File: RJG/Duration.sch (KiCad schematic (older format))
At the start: 24 parts, among them Q401 BC547, Q402 BC547, Q403 BC547, SW401 Duration Length, SW402 Reload, U101 4520, U401 4520, U402 74LS74, U403 74LS157, U404 74LS85, U405 SST39SF010, U406 74LS173

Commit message: Small improvements
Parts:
- added C402, C403, C404, C405, C406, C407: 100n, Capacitor_THT:C_Disc_D7.0mm_W2.5mm_P5.00mm, symbol Device:C
- added JP401: Overflow, symbol Jumper:SolderJumper_3_Bridged12
- renumbered JP401 to JP402, U101 to U102
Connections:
- net +5V: now also U404.2 (Ia<b), U404.3 (Ia=b), U404.4 (Ia>b), C402.2, C403.2, C404.2, C405.2, C406.2, C407.2
- net GND: now also C402.1, C403.1, C404.1, C405.1, C406.1, C407.1; no longer U404.2 (Ia<b), U404.3 (Ia=b), U404.4 (Ia>b)
- net at U404.5 (Oa>b): now also JP401.1 (A)
- net at U404.6 (Oa=b): now also JP401.3 (B); no longer C401.2
- net Rst_duration: now reaches JP402.2 (C), U102.15 (Reset)
- net at Q403.2 (B): now also R406.2; no longer R406.1
- net at C401.1, JP402.1 (A), R407.2: now also R406.1; no longer R406.2
- new net: C401.2, JP401.2 (C)
- no-connect marks 7 -> 5
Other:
- moved on the sheet: C401, JP402, Q403, R406, R407, SW401, U102B, U401C, U402C, U404

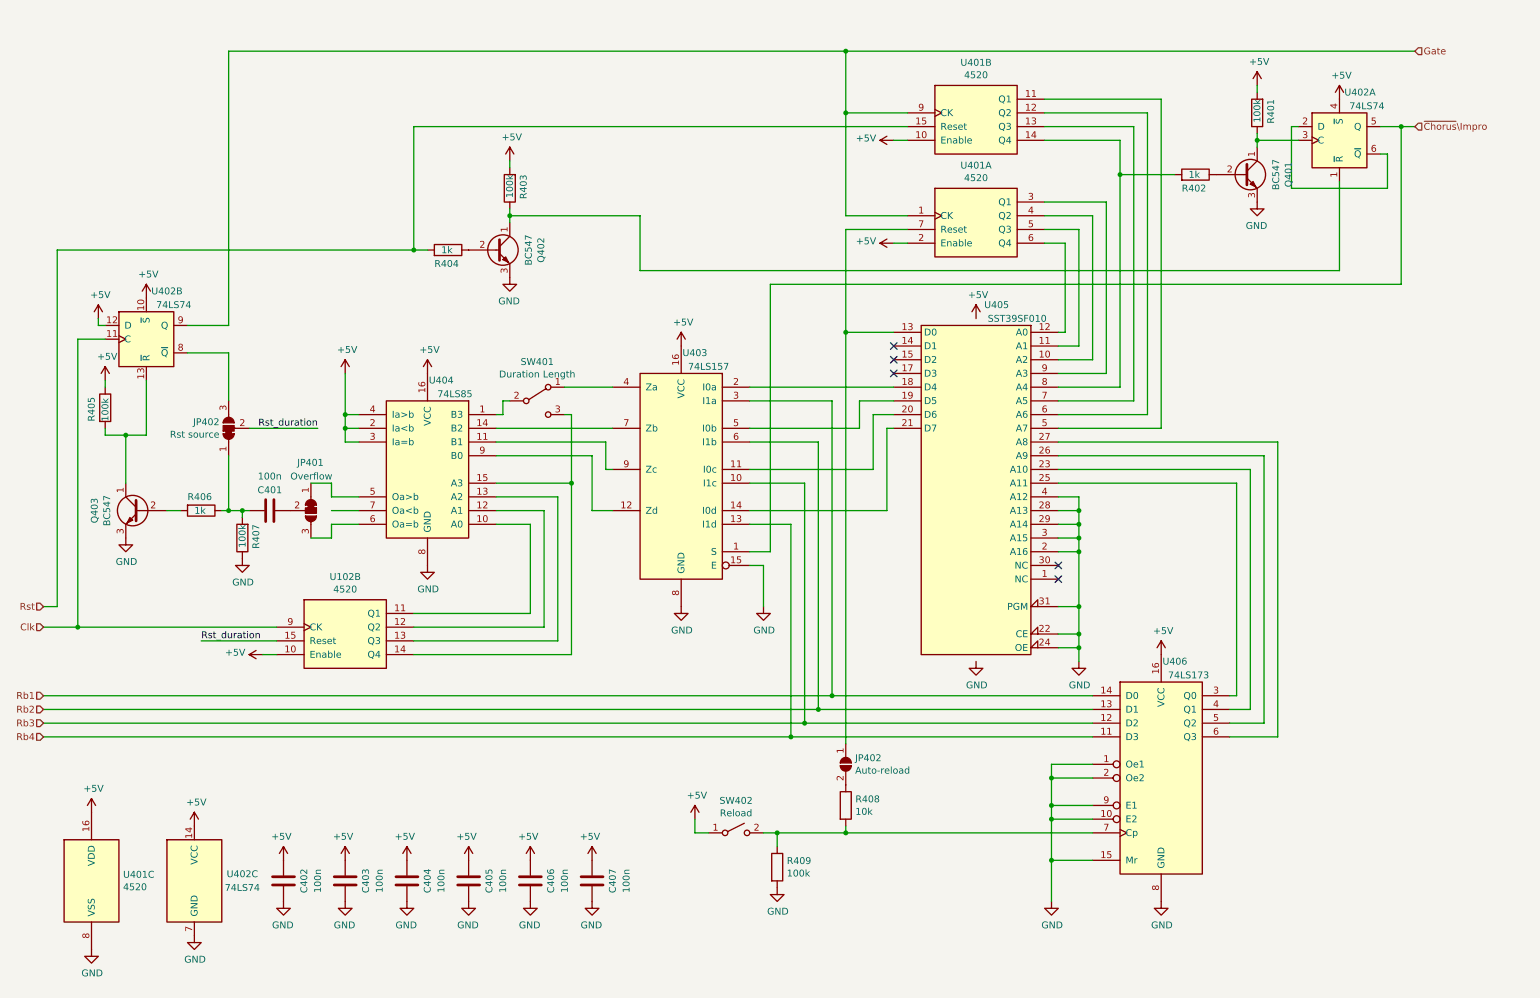
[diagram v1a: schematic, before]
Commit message: Schematic done
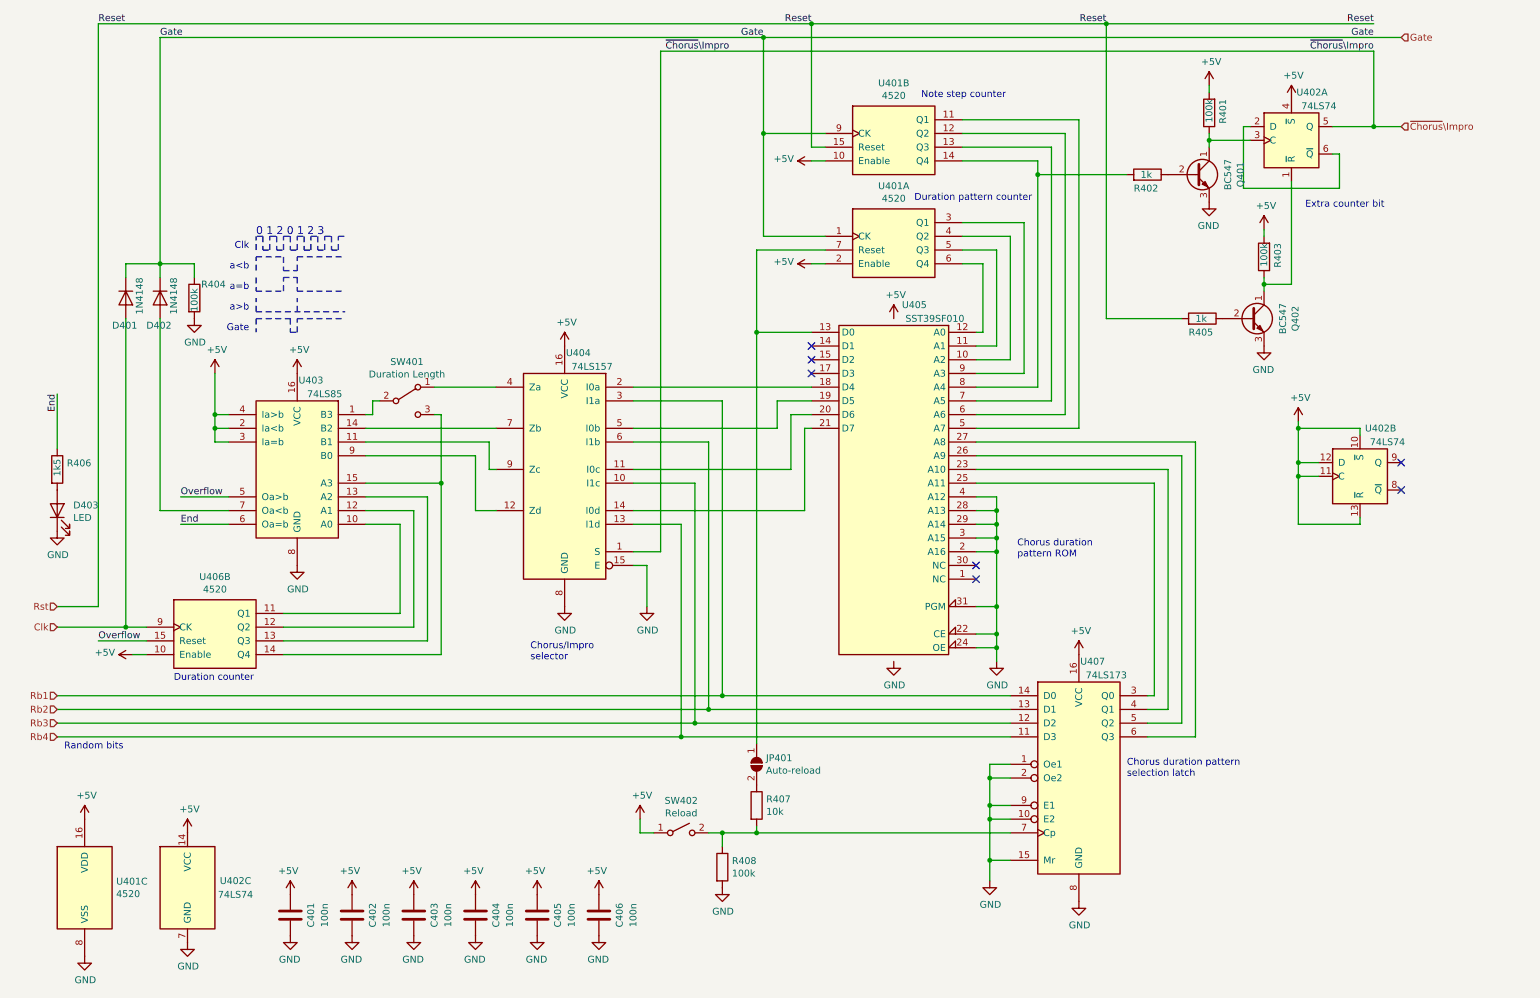
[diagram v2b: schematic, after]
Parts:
- removed C401: 100n, Capacitor_THT:C_Disc_D7.0mm_W2.5mm_P5.00mm, symbol Device:C
- removed JP401: Overflow, symbol Jumper:SolderJumper_3_Bridged12
- removed JP402: Rst source, symbol Jumper:SolderJumper_3_Bridged12
- removed Q403: BC547, Package_TO_SOT_THT:TO-92_Inline_Wide, symbol Transistor_BJT:BC547
- removed R405, R407: 100k, Resistor_THT:R_Axial_DIN0204_L3.6mm_D1.6mm_P7.62mm_Horizontal, symbol Device:R
- added D401, D402: 1N4148, Diode_THT:D_DO-35_SOD27_P7.62mm_Horizontal, symbol Device:D
- added D403: LED, LED_THT:LED_D3.0mm, symbol Device:LED
- added R404: 100k, Resistor_THT:R_Axial_DIN0204_L3.6mm_D1.6mm_P7.62mm_Horizontal, symbol Device:R
- JP401: renamed from JP402; footprint (none) -> Jumper:SolderJumper-2_P1.3mm_Open_RoundedPad1.0x1.5mm
- R406: value 1k -> 1k5
- SW401: footprint (none) -> Connector_PinHeader_2.54mm:PinHeader_1x03_P2.54mm_Vertical
- SW402: footprint (none) -> Button_Switch_THT:SW_PUSH_6mm
- renumbered C402 to C401, C403 to C402, C404 to C403, C405 to C404, C406 to C405, C407 to C406, R404 to R405, R408 to R407, R409 to R408, U404 to U403, U403 to U404, U102 to U406, U406 to U407
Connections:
- net Rst_duration is gone; now on net Overflow: U406.15 (Reset)
- net +5V: now also U402.11 (C), U402.13 (~R)
- net Clk: now also D401.2 (A); no longer U402.11 (C)
- net GND: now also D403.1 (K), R404.2
- net Gate: now also D401.1 (K), D402.1 (K), R404.1; no longer U402.9 (Q)
- net Overflow: now reaches U403.5 (Oa>b)
- net End: now reaches U403.6 (Oa=b)
- net End: now also R406.1
- net at U403.7 (Oa<b): now also D402.2 (A)
- net at R406.2: now also D403.2 (A)
- no-connect marks 5 -> 7
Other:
- note added: "0 1 2 0 1 2 3"
- note added: "Chorus duration pattern\nselection latch"
- note added: "Chorus duration\npattern ROM"
- note added: "Chorus/Impro\nselector"
- note added: "Clk"
- note added: "Duration counter"
- note added: "Duration pattern counter"
- note added: "Extra counter bit"
- note added: "Gate"
- note added: "Note step counter"
- note added: "Random bits"
- note added: "a<b"
- note added: "a=b"
- note added: "a>b"
- moved on the sheet: C401, C402, C403, C404, C405, C406, JP401, Q401, Q402, R401, R402, R403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

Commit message: Layout improvment
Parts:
- D403: footprint LED_THT:LED_D3.0mm -> LED_SMD:LED_1206_3216Metric_ReverseMount_Hole1.8x2.4mm
- R401, R403: footprint Resistor_THT:R_Axial_DIN0204_L3.6mm_D1.6mm_P7.62mm_Horizontal -> Resistor_THT:R_Axial_DIN0204_L3.6mm_D1.6mm_P2.54mm_Vertical
- R402, R405: value 1k -> 10k; footprint Resistor_THT:R_Axial_DIN0204_L3.6mm_D1.6mm_P7.62mm_Horizontal -> Resistor_THT:R_Axial_DIN0204_L3.6mm_D1.6mm_P2.54mm_Vertical
- R406: value 1k5 -> 1k; footprint Resistor_THT:R_Axial_DIN0204_L3.6mm_D1.6mm_P7.62mm_Horizontal -> Resistor_SMD:R_1206_3216Metric_Pad1.42x1.75mm_HandSolder
- U405: footprint Package_LCC:PLCC-32_11.4x14.0mm_P1.27mm -> telec:PLCC-32_THT-Socket
- renumbered U406 to U102
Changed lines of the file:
@@
 F 0 "U405" H 6700 5400 50  0000 C CNN
 F 1 "SST39SF010" H 6550 5300 50  0000 C CNN
-F 2 "Package_LCC:PLCC-32_11.4x14.0mm_P1.27mm" H 6850 4300 50  0001 C CNN
+F 2 "telec:PLCC-32_THT-Socket" H 6850 4300 50  0001 C CNN
 F 3 "http://ww1.microchip.com/downloads/en/DeviceDoc/25022B.pdf" H 6850 4300 50  0001 C CNN
 	1    6850 4000
@@
 P 1900 4950
 AR Path="/5F436EFF" Ref="U?"  Part="1"
-AR Path="/5F425067/5F436EFF" Ref="U406"  Part="2"
-F 0 "U406" H 1900 5317 50  0000 C CNN
+AR Path="/5F425067/5F436EFF" Ref="U102"  Part="2"
+F 0 "U102" H 1900 5317 50  0000 C CNN
 F 1 "4520" H 1900 5226 50  0000 C CNN
 F 2 "Package_DIP:DIP-16_W7.62mm_LongPads" H 1900 4950 50  0001 C CNN
@@
 AR Path="/5F425067/5F8F2AF1" Ref="R405"  Part="1"
 F 0 "R405" V 9000 2600 50  0000 L CNN
-F 1 "1k" V 9100 2650 50  0000 L CNN
-F 2 "Resistor_THT:R_Axial_DIN0204_L3.6mm_D1.6mm_P7.62mm_Horizontal" V 9030 2700 50  0001 C CNN
+F 1 "10k" V 9100 2650 50  0000 L CNN
+F 2 "Resistor_THT:R_Axial_DIN0204_L3.6mm_D1.6mm_P2.54mm_Vertical" V 9030 2700 50  0001 C CNN
 F 3 "~" H 9100 2700 50  0001 C CNN
 	1    9100 2700
@@
 F 0 "R403" V 9450 2150 50  0000 L CNN
 F 1 "100k" V 9550 2150 50  0000 L CNN
-F 2 "Resistor_THT:R_Axial_DIN0204_L3.6mm_D1.6mm_P7.62mm_Horizontal" V 9480 2250 50  0001 C CNN
+F 2 "Resistor_THT:R_Axial_DIN0204_L3.6mm_D1.6mm_P2.54mm_Vertical" V 9480 2250 50  0001 C CNN
 F 3 "~" H 9550 2250 50  0001 C CNN
 	1    9550 2250
@@
 AR Path="/5F425067/5FB2C32F" Ref="R402"  Part="1"
 F 0 "R402" V 8600 1550 50  0000 L CNN
-F 1 "1k" V 8700 1600 50  0000 L CNN
-F 2 "Resistor_THT:R_Axial_DIN0204_L3.6mm_D1.6mm_P7.62mm_Horizontal" V 8630 1650 50  0001 C CNN
+F 1 "10k" V 8700 1600 50  0000 L CNN
+F 2 "Resistor_THT:R_Axial_DIN0204_L3.6mm_D1.6mm_P2.54mm_Vertical" V 8630 1650 50  0001 C CNN
 F 3 "~" H 8700 1650 50  0001 C CNN
 	1    8700 1650
@@
 F 0 "R401" V 9050 1100 50  0000 L CNN
 F 1 "100k" V 9150 1100 50  0000 L CNN
-F 2 "Resistor_THT:R_Axial_DIN0204_L3.6mm_D1.6mm_P7.62mm_Horizontal" V 9080 1200 50  0001 C CNN
+F 2 "Resistor_THT:R_Axial_DIN0204_L3.6mm_D1.6mm_P2.54mm_Vertical" V 9080 1200 50  0001 C CNN
 F 3 "~" H 9150 1200 50  0001 C CNN
 	1    9150 1200
@@
 F 0 "D403" V 789 3983 50  0000 R CNN
 F 1 "LED" V 698 3983 50  0000 R CNN
-F 2 "LED_THT:LED_D3.0mm" H 750 4100 50  0001 C CNN
+F 2 "LED_SMD:LED_1206_3216Metric_ReverseMount_Hole1.8x2.4mm" H 750 4100 50  0001 C CNN
 F 3 "~" H 750 4100 50  0001 C CNN
 	1    750  4100
@@
 AR Path="/5F425067/60110003" Ref="R406"  Part="1"
 F 0 "R406" H 820 3846 50  0000 L CNN
-F 1 "1k5" V 750 3750 50  0000 L CNN
-F 2 "Resistor_THT:R_Axial_DIN0204_L3.6mm_D1.6mm_P7.62mm_Horizontal" V 680 3800 50  0001 C CNN
+F 1 "1k" V 750 3750 50  0000 L CNN
+F 2 "Resistor_SMD:R_1206_3216Metric_Pad1.42x1.75mm_HandSolder" V 680 3800 50  0001 C CNN
 F 3 "~" H 750 3800 50  0001 C CNN
 	1    750  3800

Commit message: Layout only needs the finishing touches!
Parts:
- R407: footprint Resistor_THT:R_Axial_DIN0204_L3.6mm_D1.6mm_P7.62mm_Horizontal -> Resistor_THT:R_Axial_DIN0204_L3.6mm_D1.6mm_P2.54mm_Vertical
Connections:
- net GND: now also U405.5 (A7), U405.6 (A6), U405.7 (A5), U405.8 (A4); no longer U405.2 (A16), U405.28 (A13), U405.29 (A14), U405.4 (A12)
- net Rb1: now also U404.10 (I1c); no longer U404.3 (I1a)
- net Rb3: now also U404.13 (I1d); no longer U404.10 (I1c)
- net Rb4: now also U404.3 (I1a); no longer U404.13 (I1d)
- net at U403.11 (B1): now also U404.12 (Zd); no longer U404.9 (Zc)
- net at U403.9 (B0): now also U404.4 (Za); no longer U404.12 (Zd)
- net at U404.11 (I0c): now also U405.18 (D4); no longer U405.20 (D6)
- net at U404.14 (I0d): now also U405.20 (D6); no longer U405.21 (D7)
- net at U404.2 (I0a): now also U405.21 (D7); no longer U405.18 (D4)
- net at SW401.1 (A): now also U404.9 (Zc); no longer U404.4 (Za)
- net at U407.3 (Q0): now also U405.12 (A0); no longer U405.25 (A11)
- net at U407.4 (Q1): now also U405.11 (A1); no longer U405.23 (A10)
- net at U407.5 (Q2): now also U405.9 (A3); no longer U405.26 (A9)
- net at U407.6 (Q3): now also U405.10 (A2); no longer U405.27 (A8)
- net at U401.4 (Q2): now also U405.27 (A8); no longer U405.10 (A2)
- net at U401.5 (Q3): now also U405.25 (A11); no longer U405.11 (A1)
- net at U401.6 (Q4): now also U405.23 (A10); no longer U405.12 (A0)
- net at U401.11 (Q1): now also U405.26 (A9); no longer U405.5 (A7)
- net at U401.12 (Q2): now also U405.28 (A13); no longer U405.6 (A6)
- net at U401.13 (Q3): now also U405.29 (A14); no longer U405.7 (A5)
- net at R402.2, U401.14 (Q4): now also U405.2 (A16); no longer U405.8 (A4)
- net at U401.3 (Q1): now also U405.4 (A12); no longer U405.9 (A3)
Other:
- note added: "Bit order doesn't\nreally matter -\noptimized for\nlayout"
- moved on the sheet: JP401, R407, R408, SW402

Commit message: Minor tweaks; added BOM
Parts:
- U102, U401: value 4520 -> 74HCT4520
- U402: value 74LS74 -> 74HCT74
- U403: value 74LS85 -> 74HCT85
- U404: value 74LS157 -> 74HCT157
- U406: renamed from U407; value 74LS173 -> 74HCT173
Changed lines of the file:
@@
 AR Path="/5F425067/5F4362FD" Ref="U402"  Part="1"
 F 0 "U402" H 9900 1750 50  0000 C CNN
-F 1 "74LS74" H 9950 1650 50  0000 C CNN
+F 1 "74HCT74" H 9950 1650 50  0000 C CNN
 F 2 "Package_DIP:DIP-14_W7.62mm_LongPads" H 9750 1400 50  0001 C CNN
 F 3 "74xx/74hc_hct74.pdf" H 9750 1400 50  0001 C CNN
@@
 AR Path="/5F425067/5F436309" Ref="U404"  Part="1"
 F 0 "U404" H 4350 4650 50  0000 C CNN
-F 1 "74LS157" H 4250 4550 50  0000 C CNN
+F 1 "74HCT157" H 4250 4550 50  0000 C CNN
 F 2 "Package_DIP:DIP-16_W7.62mm_LongPads" H 4450 3800 50  0001 C CNN
 F 3 "http://www.ti.com/lit/gpn/sn74LS157" H 4450 3800 50  0001 C CNN
@@
 P 8200 6050
 AR Path="/5F43630F" Ref="U?"  Part="1"
-AR Path="/5F425067/5F43630F" Ref="U407"  Part="1"
-F 0 "U407" H 8300 6900 50  0000 C CNN
-F 1 "74LS173" H 8400 6800 50  0000 C CNN
+AR Path="/5F425067/5F43630F" Ref="U406"  Part="1"
+F 0 "U406" H 8300 6900 50  0000 C CNN
+F 1 "74HCT173" H 8400 6800 50  0000 C CNN
 F 2 "Package_DIP:DIP-16_W7.62mm_LongPads" H 8200 6050 50  0001 C CNN
 F 3 "http://www.ti.com/lit/gpn/sn74LS173" H 8200 6050 50  0001 C CNN
@@
 AR Path="/5F425067/5F436321" Ref="U401"  Part="1"
 F 0 "U401" H 6850 2467 50  0000 C CNN
-F 1 "4520" H 6850 2376 50  0000 C CNN
+F 1 "74HCT4520" H 6850 2376 50  0000 C CNN
 F 2 "Package_DIP:DIP-16_W7.62mm_LongPads" H 6850 2100 50  0001 C CNN
 F 3 "http://www.intersil.com/content/dam/Intersil/documents/cd45/cd4518bms-20bms.pdf" H 6850 2100 50  0001 C CNN
@@
 AR Path="/5F425067/5F436483" Ref="U401"  Part="2"
 F 0 "U401" H 6850 1717 50  0000 C CNN
-F 1 "4520" H 6850 1626 50  0000 C CNN
+F 1 "74HCT4520" H 6850 1626 50  0000 C CNN
 F 2 "Package_DIP:DIP-16_W7.62mm_LongPads" H 6850 1350 50  0001 C CNN
 F 3 "http://www.intersil.com/content/dam/Intersil/documents/cd45/cd4518bms-20bms.pdf" H 6850 1350 50  0001 C CNN
@@
 AR Path="/5F425067/5F436EFF" Ref="U102"  Part="2"
 F 0 "U102" H 1900 5317 50  0000 C CNN
-F 1 "4520" H 1900 5226 50  0000 C CNN
+F 1 "74HCT4520" H 1900 5226 50  0000 C CNN
 F 2 "Package_DIP:DIP-16_W7.62mm_LongPads" H 1900 4950 50  0001 C CNN
 F 3 "http://www.intersil.com/content/dam/Intersil/documents/cd45/cd4518bms-20bms.pdf" H 1900 4950 50  0001 C CNN
@@
 AR Path="/5F63EA63" Ref="U?"  Part="1"
 AR Path="/5F425067/5F63EA63" Ref="U401"  Part="3"
-F 0 "U401" H 1180 6896 50  0000 L CNN
-F 1 "4520" H 1180 6805 50  0000 L CNN
+F 0 "U401" H 1000 7300 50  0000 L CNN
+F 1 "74HCT4520" H 1000 7200 50  0000 L CNN
 F 2 "Package_DIP:DIP-16_W7.62mm_LongPads" H 950 6850 50  0001 C CNN
 F 3 "http://www.intersil.com/content/dam/Intersil/documents/cd45/cd4518bms-20bms.pdf" H 950 6850 50  0001 C CNN
@@
 AR Path="/5F6489A2" Ref="U?"  Part="1"
 AR Path="/5F425067/5F6489A2" Ref="U402"  Part="3"
-F 0 "U402" H 2050 6900 50  0000 C CNN
-F 1 "74LS74" H 2050 6800 50  0000 C CNN
+F 0 "U402" H 1850 7300 50  0000 C CNN
+F 1 "74HCT74" H 1900 7200 50  0000 C CNN
 F 2 "Package_DIP:DIP-14_W7.62mm_LongPads" H 1700 6850 50  0001 C CNN
 F 3 "74xx/74hc_hct74.pdf" H 1700 6850 50  0001 C CNN
@@
 AR Path="/5F425067/60326342" Ref="U402"  Part="2"
 F 0 "U402" H 10400 4200 50  0000 C CNN
-F 1 "74LS74" H 10450 4100 50  0000 C CNN
+F 1 "74HCT74" H 10450 4100 50  0000 C CNN
 F 2 "Package_DIP:DIP-14_W7.62mm_LongPads" H 10250 3850 50  0001 C CNN
 F 3 "74xx/74hc_hct74.pdf" H 10250 3850 50  0001 C CNN
@@
 AR Path="/5F425067/5F436303" Ref="U403"  Part="1"
 F 0 "U403" H 2400 4450 50  0000 C CNN
-F 1 "74LS85" H 2300 4350 50  0000 C CNN
+F 1 "74HCT85" H 2300 4350 50  0000 C CNN
 F 2 "Package_DIP:DIP-16_W7.62mm_LongPads" H 2500 3800 50  0001 C CNN
 F 3 "http://www.ti.com/lit/gpn/sn74LS85" H 2500 3800 50  0001 C CNN

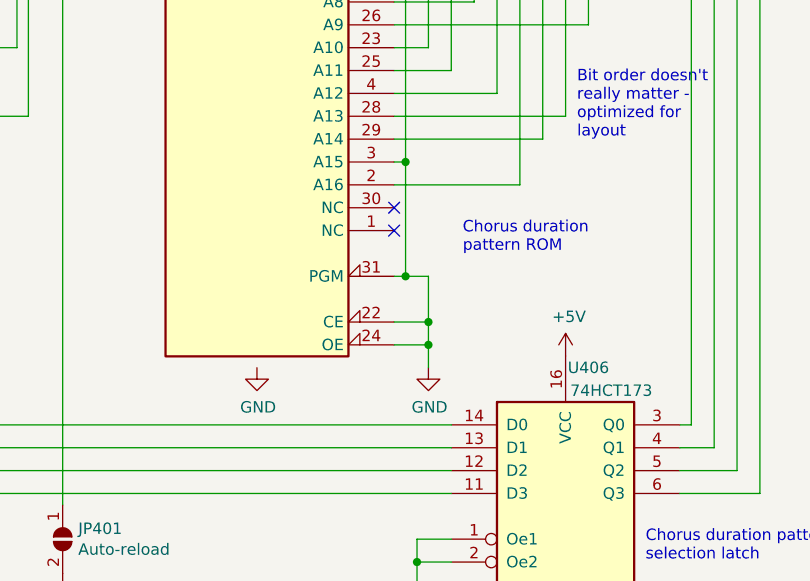
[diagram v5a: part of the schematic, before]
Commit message: fix badly connected pin
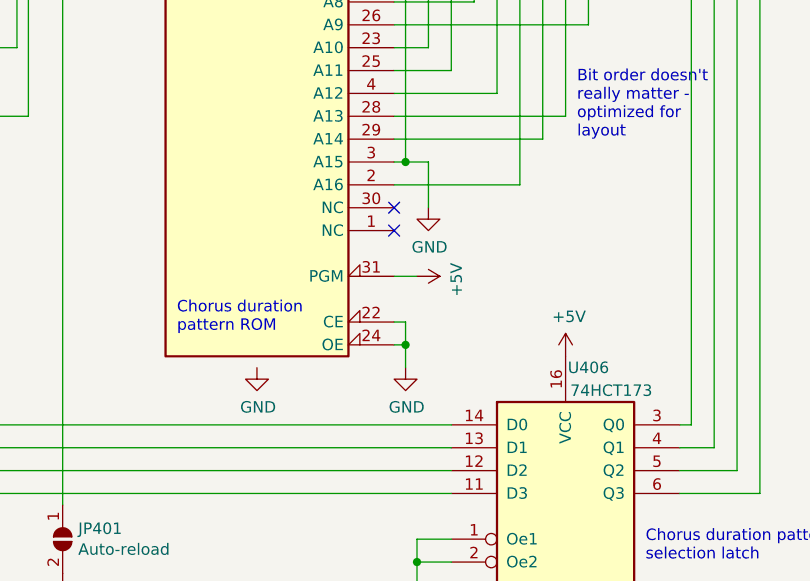
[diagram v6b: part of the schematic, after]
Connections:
- net +5V: now also U405.31 (PGM)
- net GND: no longer U405.31 (PGM)
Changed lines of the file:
@@
 L power:GND #PWR0420
 U 1 1 5F69CBD5
-P 7600 5200
-F 0 "#PWR0420" H 7600 4950 50  0001 C CNN
-F 1 "GND" H 7605 5027 50  0000 C CNN
-F 2 "" H 7600 5200 50  0001 C CNN
-F 3 "" H 7600 5200 50  0001 C CNN
-	1    7600 5200
+P 7500 5200
+F 0 "#PWR0420" H 7500 4950 50  0001 C CNN
+F 1 "GND" H 7505 5027 50  0000 C CNN
+F 2 "" H 7500 5200 50  0001 C CNN
+F 3 "" H 7500 5200 50  0001 C CNN
+	1    7500 5200
 	1    0    0    -1
 $EndComp
@@
 Gate
 Wire Wire Line
-	7450 5100 7600 5100
-Connection ~ 7600 5100
-Wire Wire Line
-	7600 5100 7600 5200
-Wire Wire Line
-	7450 5000 7600 5000
-Connection ~ 7600 5000
-Wire Wire Line
-	7600 5000 7600 5100
-Wire Wire Line
-	7450 4800 7500 4800
-Wire Wire Line
-	7600 4800 7600 5000
+	7450 5100 7500 5100
+Connection ~ 7500 5100
+Wire Wire Line
+	7500 5100 7500 5200
+Wire Wire Line
+	7450 5000 7500 5000
+Wire Wire Line
+	7500 5000 7500 5100
 $Comp
 L power:GND #PWR?
@@
 Text Notes 4200 5200 0    50   ~ 0
 Chorus/Impro\nselector
-Text Notes 7750 4700 0    50   ~ 0
+Text Notes 6500 5050 0    50   ~ 0
 Chorus duration\npattern ROM
 Text Notes 7050 1100 0    50   ~ 0
@@
 Wire Wire Line
 	7500 3200 7500 3300
-Connection ~ 7500 4800
-Wire Wire Line
-	7500 4800 7600 4800
 Wire Wire Line
 	7450 3500 7500 3500
@@
 Wire Wire Line
 	7450 4300 7500 4300
-Connection ~ 7500 4300
-Wire Wire Line
-	7500 4300 7500 4800
 Wire Wire Line
 	5800 3800 5800 3200
@@
 Text Notes 8250 4200 0    50   ~ 0
 Bit order doesn't\nreally matter -\noptimized for\nlayout
+$Comp
+L power:GND #PWR?
+U 1 1 5F42CB84
+P 7600 4500
+F 0 "#PWR?" H 7600 4250 50  0001 C CNN
+F 1 "GND" H 7605 4327 50  0000 C CNN
+F 2 "" H 7600 4500 50  0001 C CNN
+F 3 "" H 7600 4500 50  0001 C CNN
+	1    7600 4500
+	1    0    0    -1
+$EndComp
+Wire Wire Line
+	7500 4300 7600 4300
+Wire Wire Line
+	7600 4300 7600 4500
+Connection ~ 7500 4300
+$Comp
+L power:+5V #PWR?
+U 1 1 5F439D1A
+P 7550 4800
+F 0 "#PWR?" H 7550 4650 50  0001 C CNN
+F 1 "+5V" H 7565 4973 50  0000 C CNN
+F 2 "" H 7550 4800 50  0001 C CNN
+F 3 "" H 7550 4800 50  0001 C CNN
+	1    7550 4800
+	0    1    1    0
+$EndComp
+Wire Wire Line
+	7550 4800 7450 4800
 $EndSCHEMATC
